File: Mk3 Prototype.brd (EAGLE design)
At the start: 113 x 53.5 mm, 133 parts, among them IC2 CC3100, IC3 S25FL216K0PMFI011, IC4 STM32F401V, J1 ZX62-AB-5PA(11), J2 SWD_SHROUD_SMD, J7 SFV30R-2STE1HLF, Q1 BSS84W, Q11 BSS84W, Q12 2N7002KW, U1 USD-SOCKETNEW, U2 JHD12864-G13BSW-OUTLINE, U3 MCP73831, U4 ARDUINOR3-NODIM, X1 ABS07-32.768KHZ-T, X2 Q24FA20H00396, X3 CRYSTAL-3.2-2.5, X4 ABS07-32.768KHZ-T, Y1 AH316M245001-T

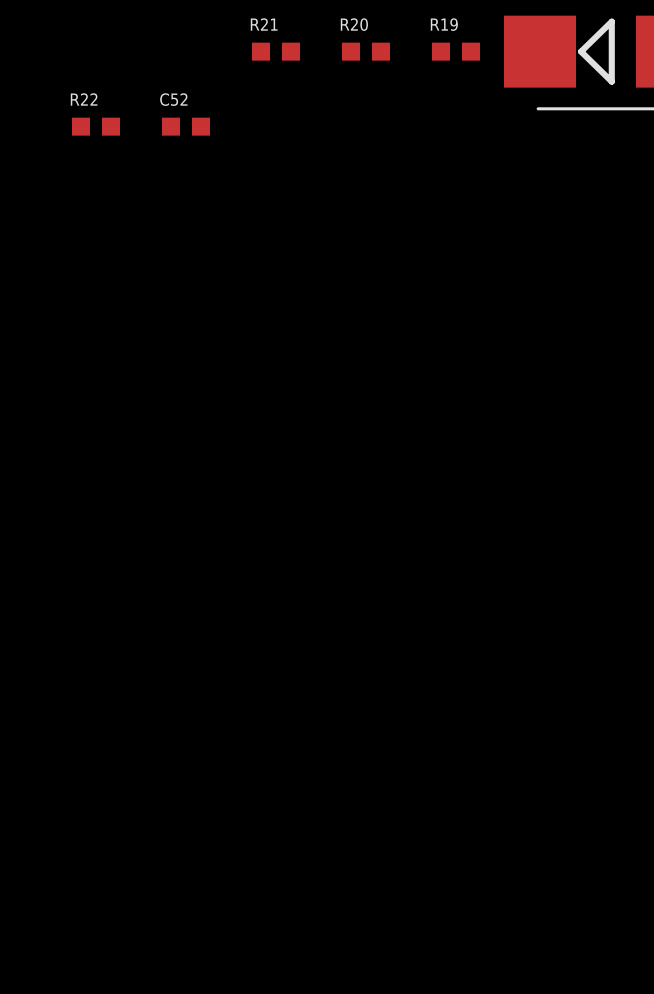
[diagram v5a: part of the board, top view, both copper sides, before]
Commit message: added servos and neopixel
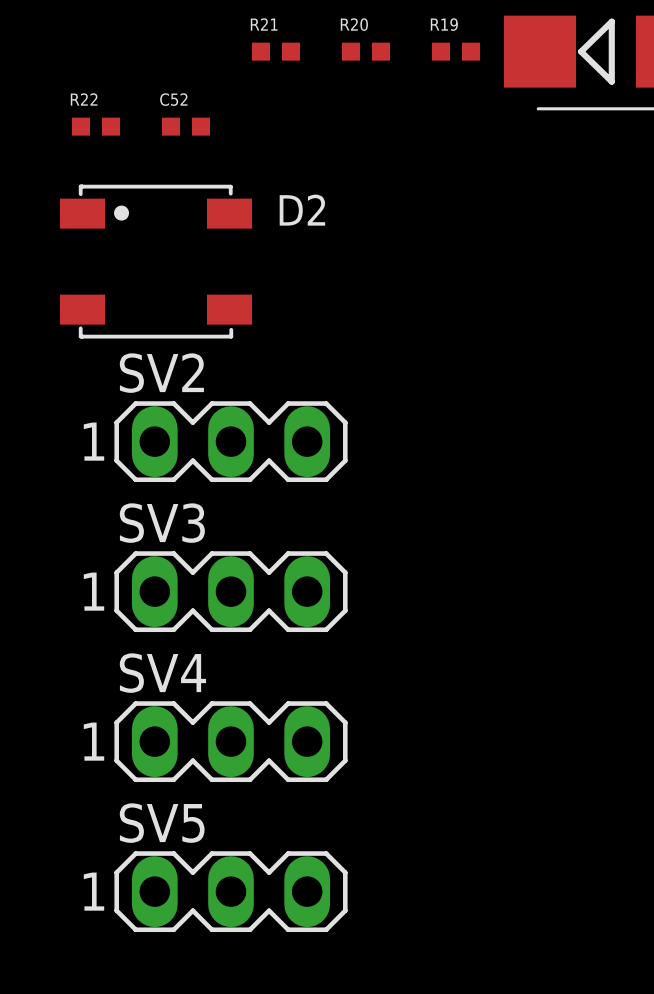
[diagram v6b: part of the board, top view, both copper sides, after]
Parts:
- added D2: (no value), SparkFun-LED:WS2812B
- added SV2, SV3, SV4, SV5: (no value), con-lstb:MA03-1
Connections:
- new net N$21: D2.2, SV1.3
- new net N$42: SV2.2, SV3.2, SV4.2, SV5.2
- new net VDD: D2.1
- net GND: now also D2.3, SV1.1, SV2.1, SV3.1, SV4.1, SV5.1
- net SPI1_MOSI: now also D2.4; no longer SV1.2
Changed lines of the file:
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@@
 <attribute name="OC_FARNELL" value="unknown" x="101" y="12" size="1.778" layer="27" rot="R90" display="off"/>
+</element>
+<element name="D2" library="SparkFun-LED" package="WS2812B" value="" x="-34.5" y="-35.5"/>
+<element name="SV2" library="con-lstb" package="MA03-1" value="" x="-32" y="-41.5">
+<attribute name="OC_NEWARK" value="unknown" x="-32" y="-41.5" size="1.778" layer="27" display="off"/>
+<attribute name="MPN" value="" x="-32" y="-41.5" size="1.778" layer="27" display="off"/>
+<attribute name="MF" value="" x="-32" y="-41.5" size="1.778" layer="27" display="off"/>
+<attribute name="OC_FARNELL" value="unknown" x="-32" y="-41.5" size="1.778" layer="27" display="off"/>
+</element>
+<element name="SV3" library="con-lstb" package="MA03-1" value="" x="-32" y="-46.5">
+<attribute name="OC_NEWARK" value="unknown" x="-32" y="-46.5" size="1.778" layer="27" display="off"/>
+<attribute name="MPN" value="" x="-32" y="-46.5" size="1.778" layer="27" display="off"/>
+<attribute name="MF" value="" x="-32" y="-46.5" size="1.778" layer="27" display="off"/>
+<attribute name="OC_FARNELL" value="unknown" x="-32" y="-46.5" size="1.778" layer="27" display="off"/>
+</element>
+<element name="SV4" library="con-lstb" package="MA03-1" value="" x="-32" y="-51.5">
+<attribute name="OC_NEWARK" value="unknown" x="-32" y="-51.5" size="1.778" layer="27" display="off"/>
+<attribute name="MPN" value="" x="-32" y="-51.5" size="1.778" layer="27" display="off"/>
+<attribute name="MF" value="" x="-32" y="-51.5" size="1.778" layer="27" display="off"/>
+<attribute name="OC_FARNELL" value="unknown" x="-32" y="-51.5" size="1.778" layer="27" display="off"/>
+</element>
+<element name="SV5" library="con-lstb" package="MA03-1" value="" x="-32" y="-56.5">
+<attribute name="OC_NEWARK" value="unknown" x="-32" y="-56.5" size="1.778" layer="27" display="off"/>
+<attribute name="MPN" value="" x="-32" y="-56.5" size="1.778" layer="27" display="off"/>
+<attribute name="MF" value="" x="-32" y="-56.5" size="1.778" layer="27" display="off"/>
+<attribute name="OC_FARNELL" value="unknown" x="-32" y="-56.5" size="1.778" layer="27" display="off"/>
 </element>
 </elements>
@@
 <contactref element="U4" pad="GND2"/>
 <contactref element="U4" pad="GND"/>
+<contactref element="D2" pad="3"/>
+<contactref element="SV1" pad="1"/>
+<contactref element="SV2" pad="1"/>
+<contactref element="SV3" pad="1"/>
+<contactref element="SV4" pad="1"/>
+<contactref element="SV5" pad="1"/>
 <wire x1="82" y1="49.5" x2="82.2" y2="51" width="0" layer="19" extent="16-16"/>
 <wire x1="81" y1="49.5" x2="82" y2="49.5" width="0" layer="19" extent="16-16"/>
@@
 <wire x1="81.5" y1="5.405" x2="84.04" y2="5.405" width="0" layer="19" extent="16-16"/>
 <wire x1="80.23" y1="5.405" x2="81.5" y2="5.405" width="0" layer="19" extent="16-16"/>
+<wire x1="101" y1="9.46" x2="94.875" y2="15.5" width="0" layer="19" extent="16-16"/>
 <wire x1="43.5" y1="27" x2="47.475" y2="36.75" width="0" layer="19" extent="16-16"/>
 <wire x1="43.65" y1="25.425" x2="43.5" y2="27" width="0" layer="19" extent="16-16"/>
@@
 <wire x1="-34" y1="-31" x2="-27" y2="-28.5" width="0" layer="19" extent="1-1"/>
 <wire x1="-36" y1="-31" x2="-34" y2="-31" width="0" layer="19" extent="1-1"/>
+<wire x1="-32.05" y1="-37.1" x2="-34" y2="-31" width="0" layer="19" extent="1-1"/>
+<wire x1="-34.54" y1="-41.5" x2="-32.05" y2="-37.1" width="0" layer="19" extent="1-1"/>
+<wire x1="-34.54" y1="-46.5" x2="-34.54" y2="-41.5" width="0" layer="19" extent="1-1"/>
+<wire x1="-34.54" y1="-51.5" x2="-34.54" y2="-46.5" width="0" layer="19" extent="1-1"/>
+<wire x1="-34.54" y1="-56.5" x2="-34.54" y2="-51.5" width="0" layer="19" extent="1-1"/>
 </signal>
 <signal name="VIN">
@@
 <signal name="SPI1_MOSI">
 <contactref element="IC4" pad="32"/>
-<contactref element="SV1" pad="2"/>
 <wire x1="34" y1="16.75" x2="34" y2="1.5" width="0.2" layer="16"/>
 <wire x1="34" y1="1.5" x2="34.5" y2="1" width="0.2" layer="16"/>
@@
 <wire x1="90.5" y1="2.5" x2="90.5" y2="7" width="0.2" layer="16"/>
 <wire x1="90.5" y1="7" x2="94.5" y2="11" width="0.2" layer="16"/>
-<wire x1="94.5" y1="11" x2="101" y2="12" width="0" layer="19" extent="16-16"/>
+<contactref element="D2" pad="4"/>
+<wire x1="34" y1="1.5" x2="-32.05" y2="-33.9" width="0" layer="19" extent="1-16"/>
 </signal>
 <signal name="USART2_TX">
@@
 <wire x1="28" y1="41.75" x2="32.62" y2="51.05" width="0" layer="19" extent="1-16"/>
 </signal>
+<signal name="VDD">
+<contactref element="D2" pad="1"/>
+</signal>
+<signal name="N$21">
+<contactref element="SV1" pad="3"/>
+<contactref element="D2" pad="2"/>
+<wire x1="-36.95" y1="-37.1" x2="101" y2="14.54" width="0" layer="19" extent="1-1"/>
+</signal>
+<signal name="N$42">
+<contactref element="SV5" pad="2"/>
+<contactref element="SV2" pad="2"/>
+<contactref element="SV3" pad="2"/>
+<contactref element="SV4" pad="2"/>
+<wire x1="-32" y1="-51.5" x2="-32" y2="-56.5" width="0" layer="19" extent="1-1"/>
+<wire x1="-32" y1="-46.5" x2="-32" y2="-51.5" width="0" layer="19" extent="1-1"/>
+<wire x1="-32" y1="-41.5" x2="-32" y2="-46.5" width="0" layer="19" extent="1-1"/>
+</signal>
 </signals>

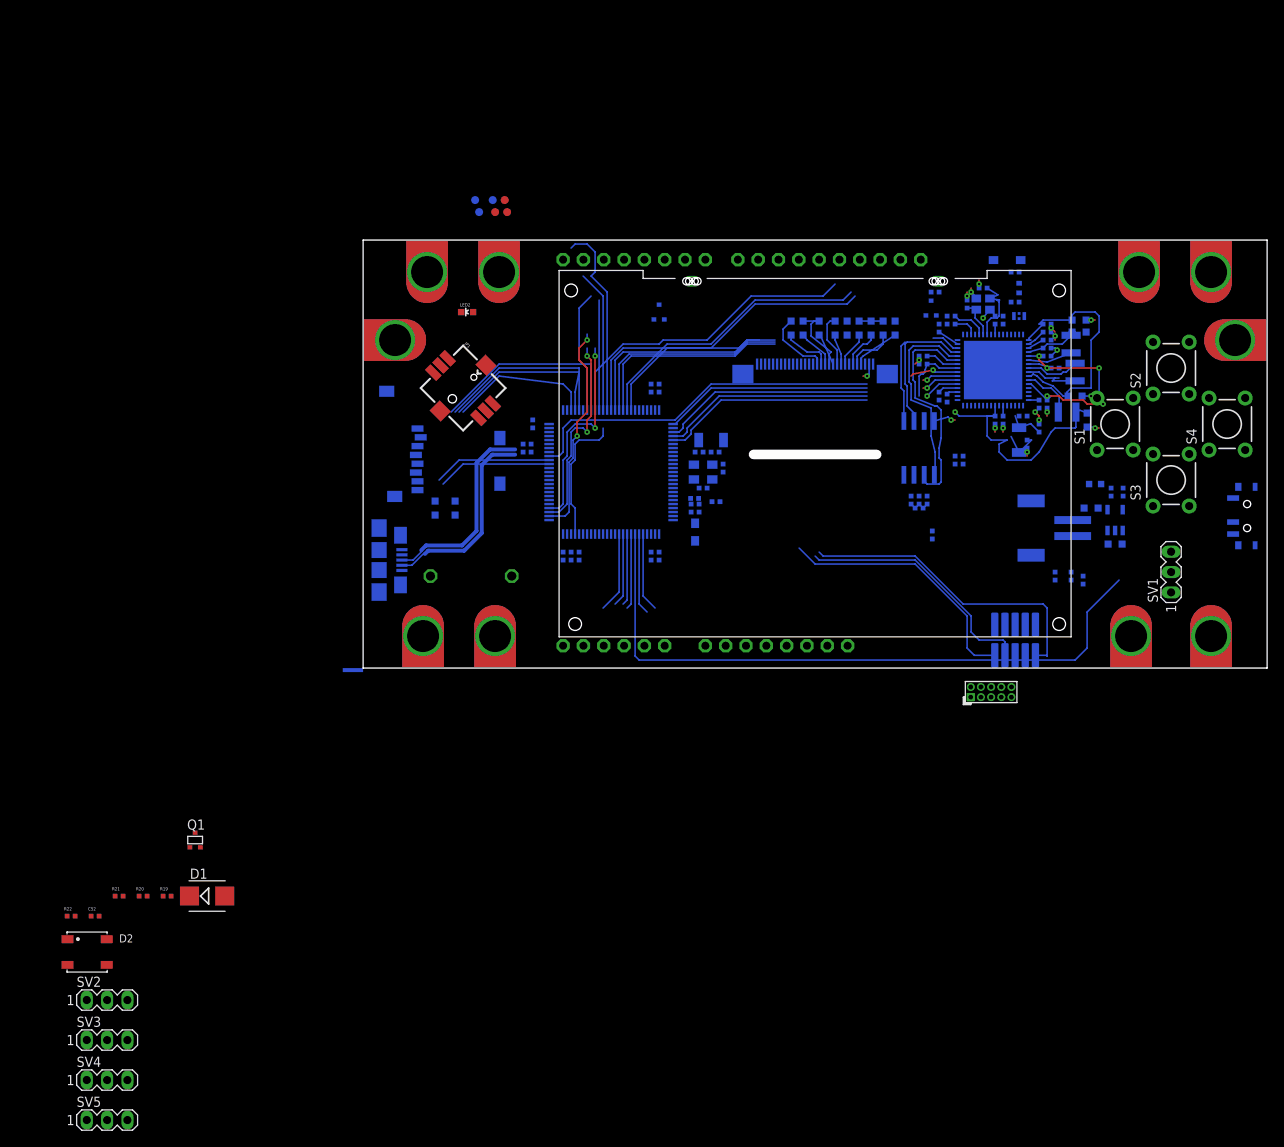
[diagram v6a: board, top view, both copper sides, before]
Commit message: wired servos and a few control signals
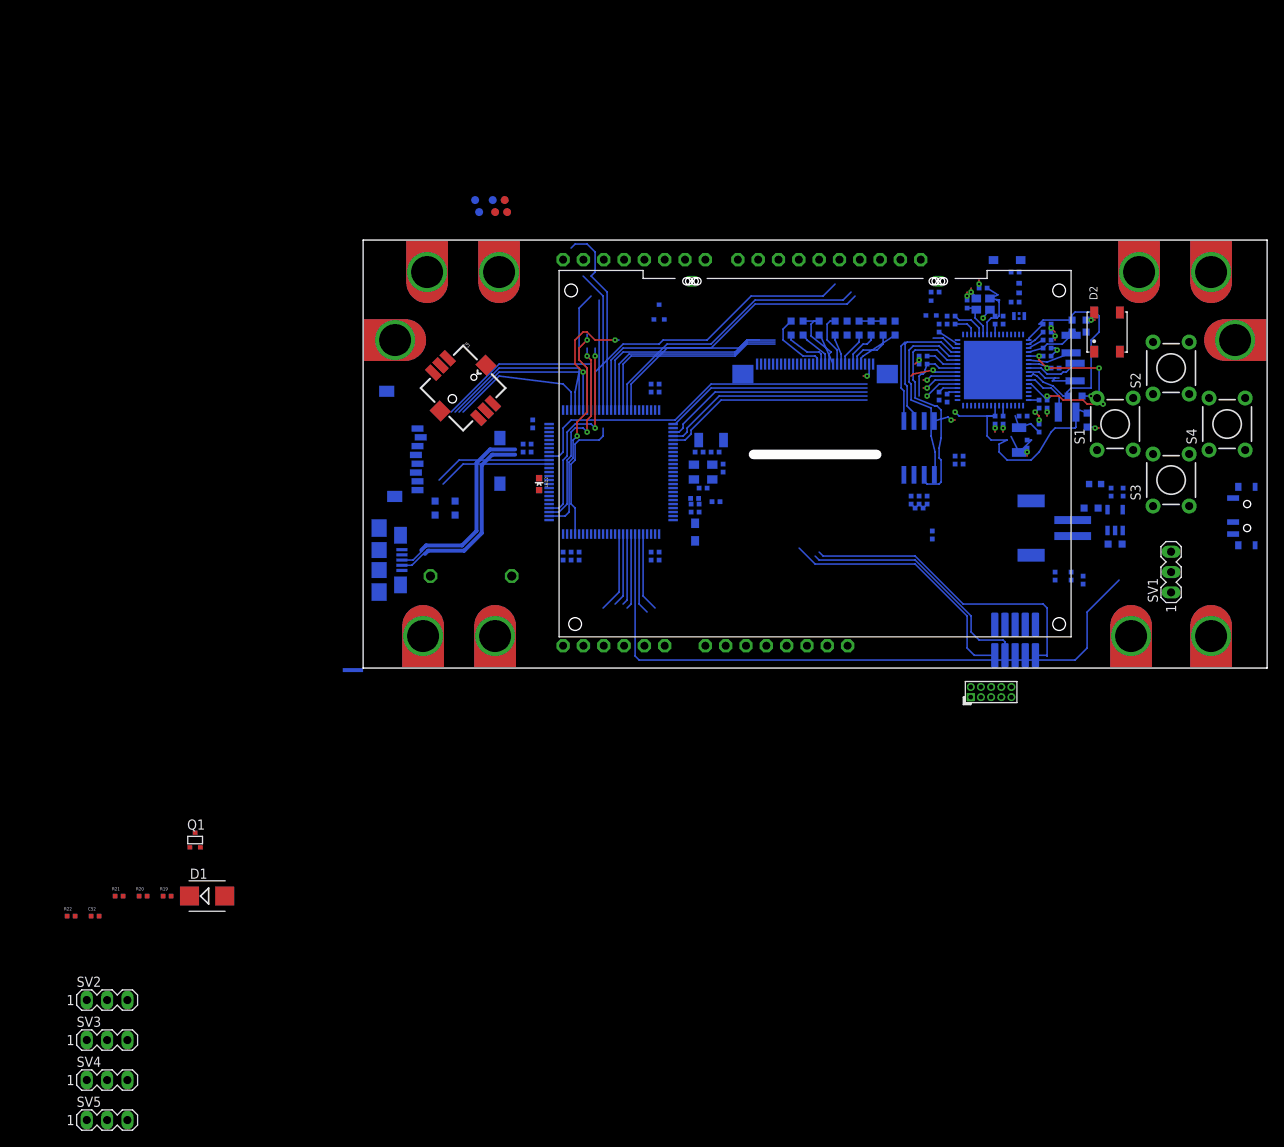
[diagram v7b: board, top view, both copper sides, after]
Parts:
- moved D2 149.2 mm to (93.0, 42.0), turned to 90 degrees
- moved LED2 23.3 mm to (22.0, 23.0), turned to 270 degrees
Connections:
- removed net N$56: IC4.64
- new net TIM1_CH1: IC4.40, SV2.3
- new net TIM1_CH2: IC4.42, SV3.3
- new net TIM1_CH3: IC4.44, SV4.3
- new net TIM1_CH4: IC4.45, SV5.3
- net LCD_!RST: now also IC4.81
- net SDIO_SW: now also IC4.64; no longer IC4.7
- net WIFI_!HIB: now also IC4.7
- net WIFI_INTR: now also IC4.2
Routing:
- net LCD_!RST: track 0.00 -> 15.5 mm, vias 0 -> 2

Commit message: adding esp, bit more wiring
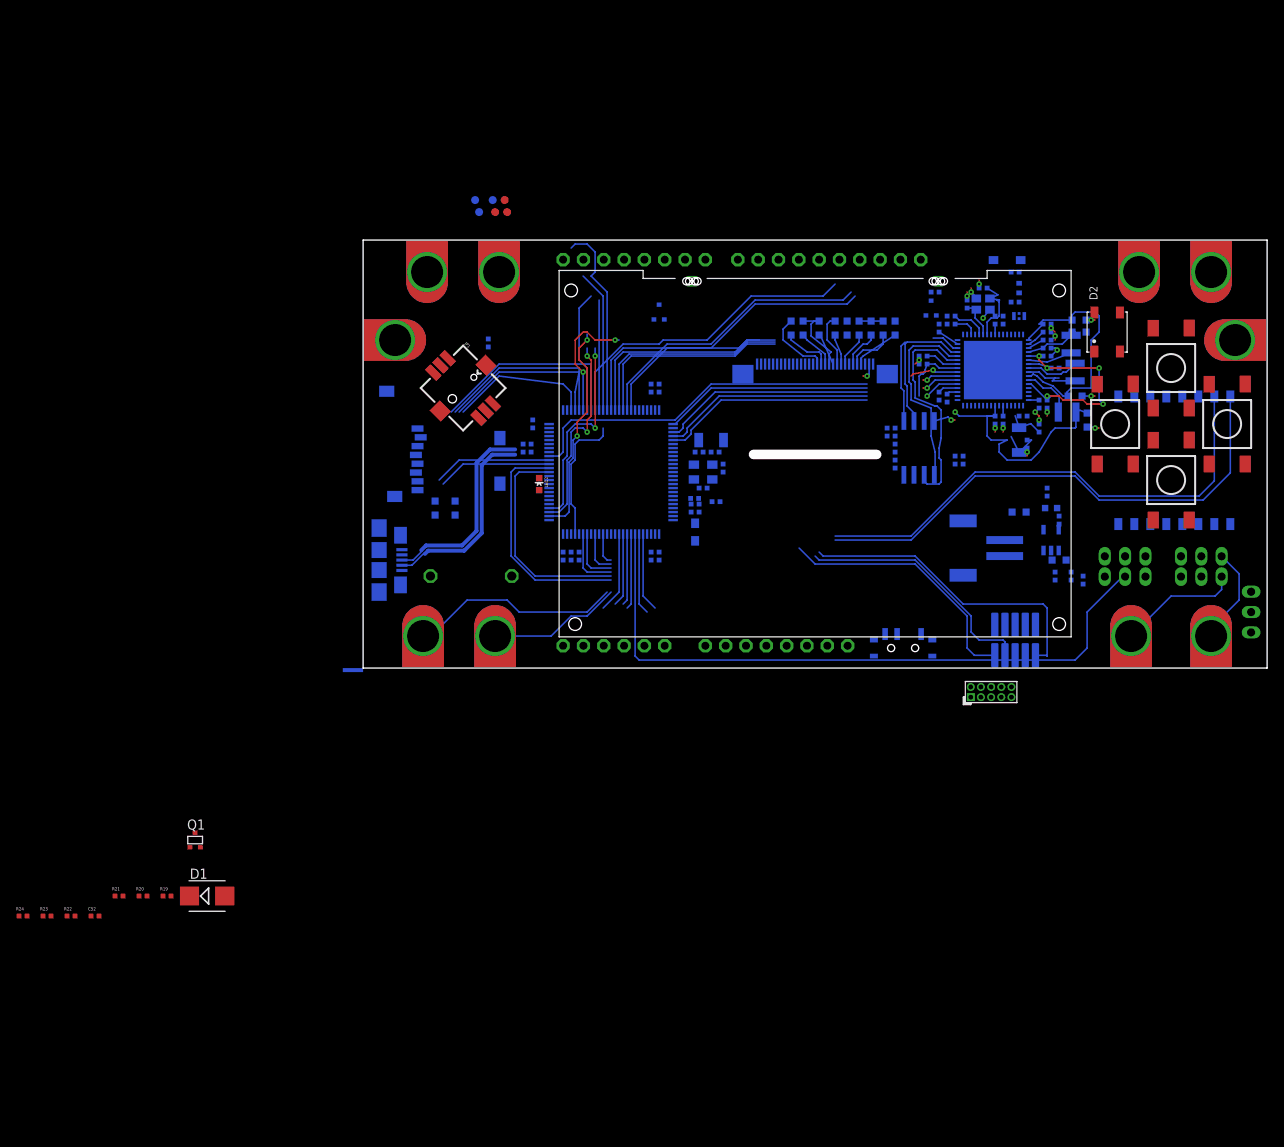
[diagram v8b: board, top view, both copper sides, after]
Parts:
- added R23, R24: 0402/100K/5%, TiLDA Mk3 Parts:R0402-SMALLER
- added X5: ESP-07, TiLDA Mk3 Parts:ESP-07
- S1, S2, S3, S4: value (none) -> SWITCH-MOMENTARY-2; device TiLDA Mk3 Parts:TACTILE-PTH -> Mine:TACTILE_SWITCH_TALL
- moved SV5 153.9 mm to (104.8, 14.0), flipped to the bottom, turned to 180 degrees
- moved SV4 150.6 mm to (104.8, 11.4), flipped to the bottom, turned to 180 degrees
- moved SV3 140.9 mm to (95.2, 14.0), flipped to the bottom, turned to 180 degrees
- moved SV2 137.8 mm to (95.2, 11.4), flipped to the bottom, turned to 180 degrees
- moved R14 60.5 mm to (15.6, 40.6)
- moved S5 46.1 mm to (67.5, 2.50), turned to 180 degrees
- moved SV1 11.2 mm to (111.0, 7.00), flipped to the bottom
- moved R3 10.3 mm to (65.5, 29.5), turned to 90 degrees
- moved R17 9.50 mm to (85.5, 22.0)
- moved R1 9.39 mm to (66.5, 29.5)
- moved C37 9.01 mm to (82.0, 19.5)
- moved JP2 8.86 mm to (76.5, 15.0)
- moved U3 8.38 mm to (86.0, 16.0)
- moved R18 7.38 mm to (87.0, 18.5)
- moved C38 7.28 mm to (87.0, 13.5)
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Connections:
- removed net N$55: IC4.63
- new net JOY_CEN: JP1.C
- new net JOY_DWN: JP1.D
- new net JOY_LEFT: JP1.B
- new net JOY_UP: JP1.A
- new net N$39: R23.2, X5.11
- new net N$43: X5.12
- new net N$44: R24.2, X5.10
- new net N$45: X5.4
- new net N$49: X5.3
- new net USART6_RX: IC4.64, X5.16
- new net USART6_TX: IC4.63, X5.15
- net +3V3: now also JP1.GND, R23.1, TP8.P$1, X5.8
- net BOOT0: now also JP1.CTR
- net GND: now also R24.1, TP6.P$1, X5.9
- net SDIO_SW: now also IC4.62; no longer IC4.64
- net TIM1_CH1: now also TP7.P$1
- net TIM1_CH2: now also TP5.P$1
- net TIM1_CH3: now also TP9.P$1
- net TIM1_CH4: now also TP10.P$1
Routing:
- net USART6_RX: track 0.00 -> 94.1 mm
- net USART6_TX: track 0.00 -> 90.8 mm
- net TIM1_CH1: track 0.00 -> 30.5 mm
- net TIM1_CH3: track 0.00 -> 22.3 mm
- net TIM1_CH2: track 0.00 -> 22.2 mm
- net TIM1_CH4: track 0.00 -> 20.3 mm
